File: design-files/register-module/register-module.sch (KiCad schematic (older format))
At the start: 134 parts, among them U201 74HCT377, U202 74HCT245, U203 AT28C64, U204 WL-T7DS-157136V12701, U205 WL-T7DS-157136V12701, U206 WL-T7DS-157136V12701, U207 WL-T7DS-157136V12701, U208 74HCT139, U209 74HCT377, U210 74HCT245, U211 AT28C64, U212 WL-T7DS-157136V12701, U213 WL-T7DS-157136V12701, U214 WL-T7DS-157136V12701, U215 WL-T7DS-157136V12701, U216 74HCT377, U217 74HCT245, U218 AT28C64, U219 WL-T7DS-157136V12701, U220 WL-T7DS-157136V12701, U221 WL-T7DS-157136V12701, U222 WL-T7DS-157136V12701, U223 74HCT139, U224 74HCT377, U225 74HCT245, U226 AT28C64, U227 WL-T7DS-157136V12701, U228 WL-T7DS-157136V12701, U229 WL-T7DS-157136V12701, U230 WL-T7DS-157136V12701, U231 74HCT161, U232 NE555P

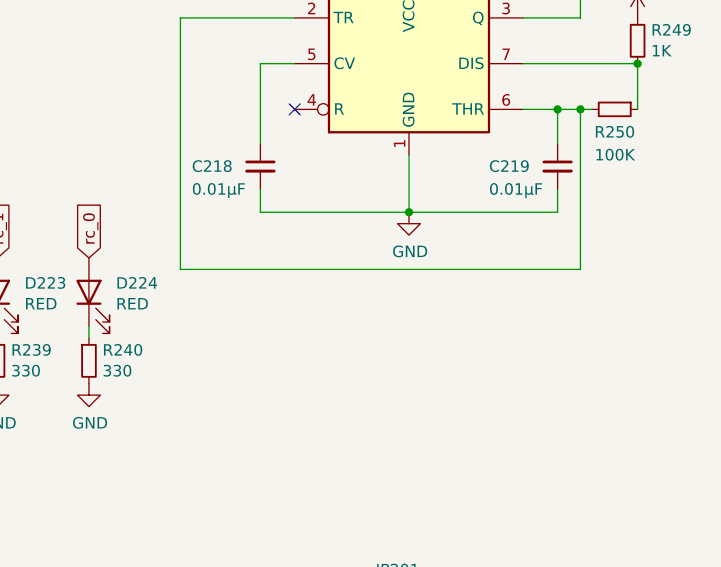
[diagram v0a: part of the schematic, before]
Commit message: register-module: Document the nominal frequency of the display mux clock.
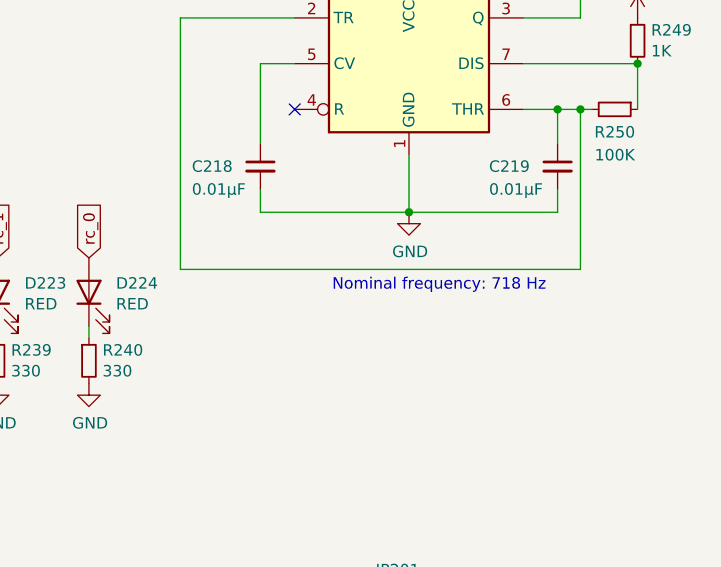
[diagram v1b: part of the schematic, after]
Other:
- note added: "Nominal frequency: 718 Hz"
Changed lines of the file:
@@
 Wire Wire Line
 	13400 1350 13400 1400
+Text Notes 15400 6050 2    50   ~ 0
+Nominal frequency: 718 Hz
 $EndSCHEMATC

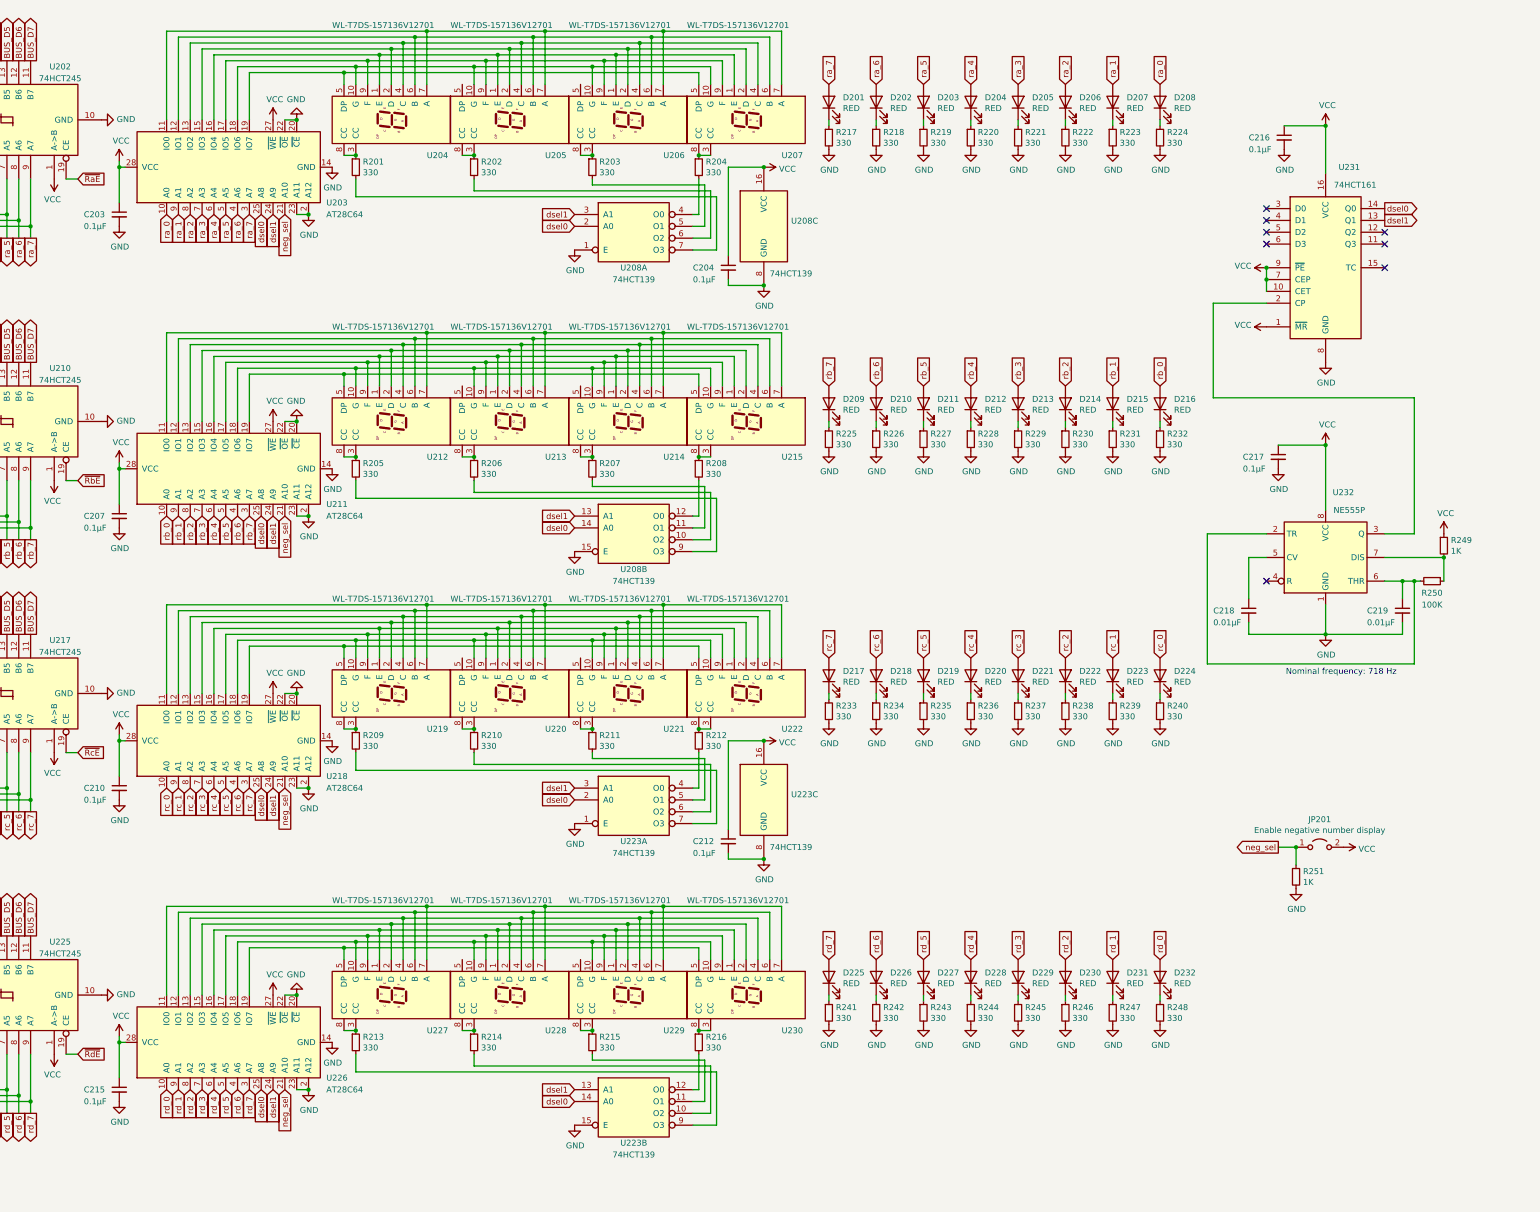
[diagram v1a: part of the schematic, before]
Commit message: Rework to use DIP resistor packs for the LEDs.
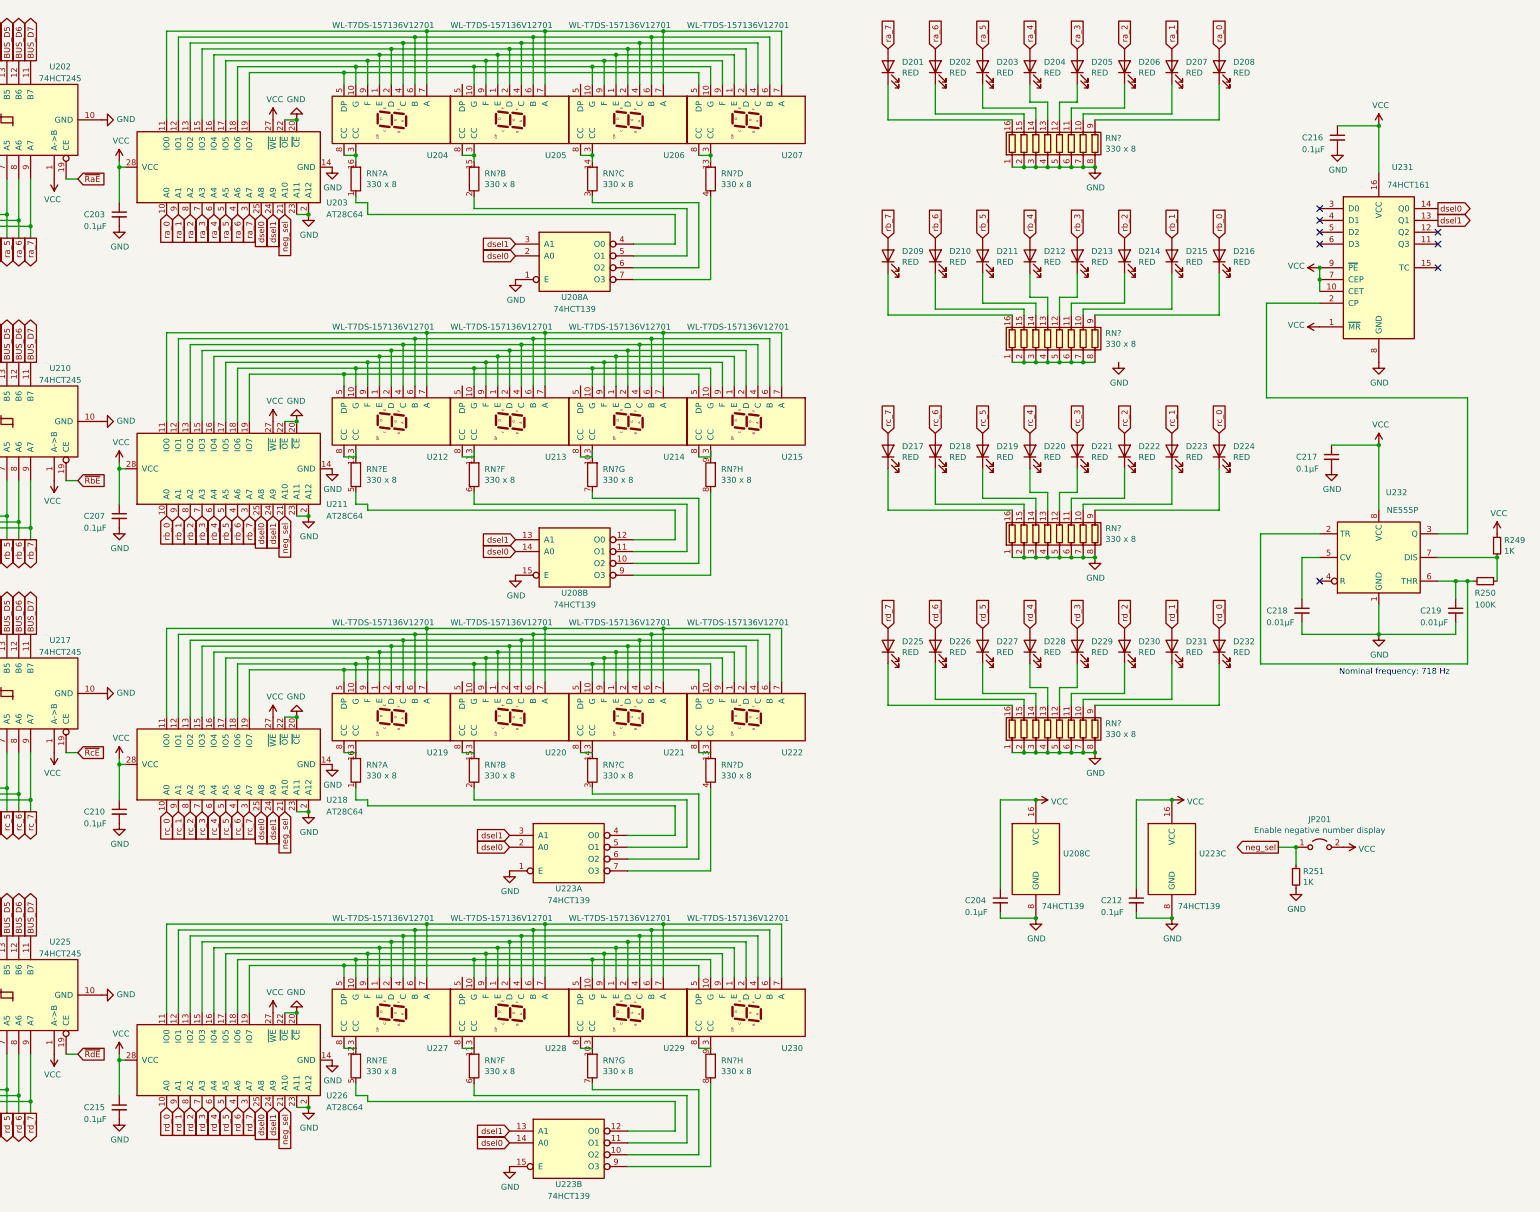
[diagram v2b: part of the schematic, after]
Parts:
- removed R201, R202, R203, R204, R205, R206, R207, R208, R209, R210, R211, R212, R213, R214, R215, R216, R217, R218, R219, R220, R221, R222, R223, R224, R225, R226, R227, R228, R229, R230, R231, R232, R233, R234, R235, R236, R237, R238, R239, R240, R241, R242, R243, R244, R245, R246, R247, R248: 330, Resistor_THT:R_Axial_DIN0204_L3.6mm_D1.6mm_P5.08mm_Horizontal, symbol Device:R_Small
- added RN? (x4): 330 x 8, Package_DIP:DIP-16_W7.62mm_Socket, symbol Device:R_Pack08
- added RN? (x16): 330 x 8, Package_DIP:DIP-16_W7.62mm_Socket, symbol Device:R_Pack08_Split
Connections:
- net GND: now also RN?.1 (R1.1), RN?.1 (R1.1), RN?.1 (R1.1), RN?.2 (R2.1), RN?.2 (R2.1), RN?.2 (R2.1), RN?.3 (R3.1), RN?.3 (R3.1), RN?.3 (R3.1), RN?.4 (R4.1), RN?.4 (R4.1), RN?.4 (R4.1), RN?.5 (R5.1), RN?.5 (R5.1), RN?.5 (R5.1), RN?.6 (R6.1), RN?.6 (R6.1), RN?.6 (R6.1), RN?.7 (R7.1), RN?.7 (R7.1), RN?.7 (R7.1), RN?.8 (R8.1), RN?.8 (R8.1), RN?.8 (R8.1)
- net at U207.3 (CC), U207.8 (CC): now also RN?.13 (R4.2)
- net at U206.3 (CC), U206.8 (CC): now also RN?.14 (R3.2)
- net at U205.3 (CC), U205.8 (CC): now also RN?.15 (R2.2)
- net at U204.3 (CC), U204.8 (CC): now also RN?.16 (R1.2)
- net at U208.4 (O0): now also RN?.1 (R1.1)
- net at U208.5 (O1): now also RN?.2 (R2.1)
- net at U208.6 (O2): now also RN?.3 (R3.1)
- net at U208.7 (O3): now also RN?.4 (R4.1)
- net at U215.3 (CC), U215.8 (CC): now also RN?.9 (R8.2)
- net at U214.3 (CC), U214.8 (CC): now also RN?.10 (R7.2)
- net at U213.3 (CC), U213.8 (CC): now also RN?.11 (R6.2)
- net at U212.3 (CC), U212.8 (CC): now also RN?.12 (R5.2)
- net at U208.10 (O2): now also RN?.7 (R7.1)
- net at U208.11 (O1): now also RN?.6 (R6.1)
- net at U208.12 (O0): now also RN?.5 (R5.1)
- net at U208.9 (O3): now also RN?.8 (R8.1)
- net at D201.1 (K): now also RN?.16 (R1.2)
- net at D202.1 (K): now also RN?.15 (R2.2)
- net at D203.1 (K): now also RN?.14 (R3.2)
- net at D204.1 (K): now also RN?.13 (R4.2)
- net at D205.1 (K): now also RN?.12 (R5.2)
- net at D206.1 (K): now also RN?.11 (R6.2)
- net at D207.1 (K): now also RN?.10 (R7.2)
- net at D208.1 (K): now also RN?.9 (R8.2)
- net at D209.1 (K): now also RN?.16 (R1.2)
- net at D210.1 (K): now also RN?.15 (R2.2)
- net at D211.1 (K): now also RN?.14 (R3.2)
- net at D212.1 (K): now also RN?.13 (R4.2)
- net at D213.1 (K): now also RN?.12 (R5.2)
- net at D214.1 (K): now also RN?.11 (R6.2)
- net at D215.1 (K): now also RN?.10 (R7.2)
- net at D216.1 (K): now also RN?.9 (R8.2)
- net at U222.3 (CC), U222.8 (CC): now also RN?.13 (R4.2)
- net at U221.3 (CC), U221.8 (CC): now also RN?.14 (R3.2)
- net at U220.3 (CC), U220.8 (CC): now also RN?.15 (R2.2)
- net at U219.3 (CC), U219.8 (CC): now also RN?.16 (R1.2)
- net at U223.4 (O0): now also RN?.1 (R1.1)
- net at U223.5 (O1): now also RN?.2 (R2.1)
- net at U223.6 (O2): now also RN?.3 (R3.1)
- net at U223.7 (O3): now also RN?.4 (R4.1)
- net at U230.3 (CC), U230.8 (CC): now also RN?.9 (R8.2)
- net at U229.3 (CC), U229.8 (CC): now also RN?.10 (R7.2)
- net at U228.3 (CC), U228.8 (CC): now also RN?.11 (R6.2)
- net at U227.3 (CC), U227.8 (CC): now also RN?.12 (R5.2)
- net at U223.10 (O2): now also RN?.7 (R7.1)
- net at U223.11 (O1): now also RN?.6 (R6.1)
- net at U223.12 (O0): now also RN?.5 (R5.1)
- net at U223.9 (O3): now also RN?.8 (R8.1)
- net at D217.1 (K): now also RN?.16 (R1.2)
- net at D218.1 (K): now also RN?.15 (R2.2)
- net at D219.1 (K): now also RN?.14 (R3.2)
- net at D220.1 (K): now also RN?.13 (R4.2)
- net at D221.1 (K): now also RN?.12 (R5.2)
- net at D222.1 (K): now also RN?.11 (R6.2)
- net at D223.1 (K): now also RN?.10 (R7.2)
- net at D224.1 (K): now also RN?.9 (R8.2)
- net at D225.1 (K): now also RN?.16 (R1.2)
- net at D226.1 (K): now also RN?.15 (R2.2)
- net at D227.1 (K): now also RN?.14 (R3.2)
- net at D228.1 (K): now also RN?.13 (R4.2)
- net at D229.1 (K): now also RN?.12 (R5.2)
- net at D230.1 (K): now also RN?.11 (R6.2)
- net at D231.1 (K): now also RN?.10 (R7.2)
- net at D232.1 (K): now also RN?.9 (R8.2)
- new net: RN?.1 (R1.1), RN?.2 (R2.1), RN?.3 (R3.1), RN?.4 (R4.1), RN?.5 (R5.1), RN?.6 (R6.1), RN?.7 (R7.1), RN?.8 (R8.1)
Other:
- moved on the sheet: C204, C210, C212, C215, C216, C217, C218, C219, D201, D202, D203, D204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
